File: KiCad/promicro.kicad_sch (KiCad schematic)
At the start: 60 parts, among them J1 918-418K2024S40000, J2 Conn_01x13_Pin, J3 Conn_01x13_Pin, J4 Conn_01x03_Pin, Q1 AO3401A, U1 nRF52840, U2 ME6217, U3 TP4054, U4 USBLC6-2P6, Y1 32 MHz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

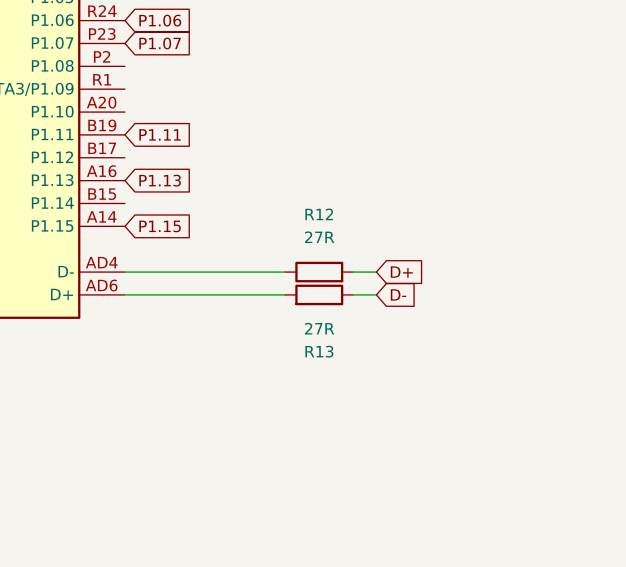
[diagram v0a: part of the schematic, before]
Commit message: Fix USB pins
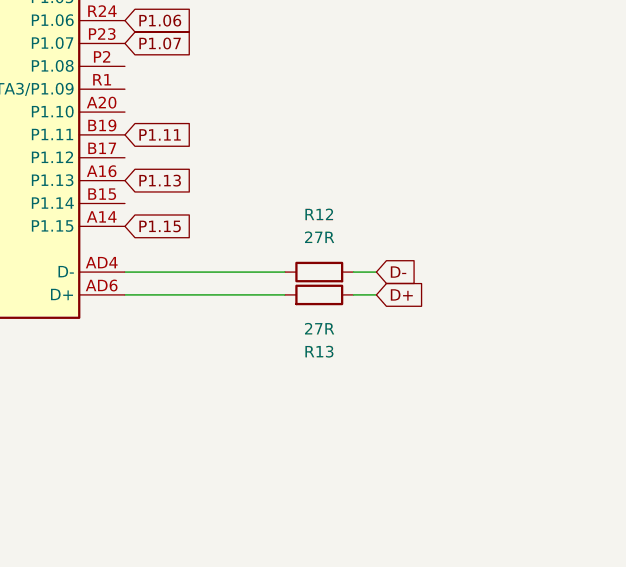
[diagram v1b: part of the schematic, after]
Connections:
- net D+: now also R13.1; no longer R12.2
- net D-: now also R12.2; no longer R13.1
